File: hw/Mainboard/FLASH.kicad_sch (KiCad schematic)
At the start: 5 parts, among them J8 FLASH, U16 W25Q128JVS

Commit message: hw: add more Mouse part numbers
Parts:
- J8: MOUSER (none) -> 649-1012937893602BLF
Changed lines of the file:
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@@
+      (effects (font (size 1.27 1.27)) hide)
+    )
+    (property "MOUSER" "649-1012937893602BLF" (id 4) (at 107.95 114.3 0)
       (effects (font (size 1.27 1.27)) hide)
     )

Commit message: hw: 9V DC plug on left edge, change default track size
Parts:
- renumbered C51 to C85, J8 to J26, R25 to R72, R26 to R73, U16 to U22
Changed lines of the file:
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@@
   (symbol (lib_id "power:GND") (at 142.24 115.57 0) (unit 1)
     (in_bom yes) (on_board yes) (fields_autoplaced)
-    (property "Reference" "#PWR079" (id 0) (at 142.24 121.92 0)
+    (property "Reference" "#PWR0156" (id 0) (at 142.24 121.92 0)
       (effects (font (size 1.27 1.27)) hide)
     )
@@
   (symbol (lib_id "Device:R_Small") (at 127 88.9 0) (unit 1)
     (in_bom yes) (on_board yes)
-    (property "Reference" "R25" (id 0) (at 125.095 90.805 90)
+    (property "Reference" "R72" (id 0) (at 125.095 90.805 90)
       (effects (font (size 1.27 1.27)) (justify left))
     )
@@
   (symbol (lib_id "power:+3V3") (at 127 85.09 0) (unit 1)
     (in_bom yes) (on_board yes) (fields_autoplaced)
-    (property "Reference" "#PWR077" (id 0) (at 127 88.9 0)
+    (property "Reference" "#PWR0155" (id 0) (at 127 88.9 0)
       (effects (font (size 1.27 1.27)) hide)
     )
@@
   (symbol (lib_id "Device:R_Small") (at 116.84 101.6 180) (unit 1)
     (in_bom yes) (on_board yes)
-    (property "Reference" "R26" (id 0) (at 114.935 99.695 90)
+    (property "Reference" "R73" (id 0) (at 114.935 99.695 90)
       (effects (font (size 1.27 1.27)) (justify left))
     )
@@
   (symbol (lib_id "Device:C_Small") (at 146.05 78.74 0) (unit 1)
     (in_bom yes) (on_board yes)
-    (property "Reference" "C51" (id 0) (at 148.3868 77.5716 0)
+    (property "Reference" "C85" (id 0) (at 148.3868 77.5716 0)
       (effects (font (size 1.27 1.27)) (justify left))
     )
@@
   (symbol (lib_id "Memory_Flash:W25Q128JVS") (at 142.24 96.52 0) (unit 1)
     (in_bom yes) (on_board yes)
-    (property "Reference" "U16" (id 0) (at 133.35 87.63 0)
+    (property "Reference" "U22" (id 0) (at 133.35 87.63 0)
       (effects (font (size 1.27 1.27)) (justify left))
     )
@@
   (symbol (lib_id "Connector:Conn_01x02_Male") (at 107.95 114.3 0) (mirror x) (unit 1)
     (in_bom yes) (on_board yes) (fields_autoplaced)
-    (property "Reference" "J8" (id 0) (at 106.68 111.7599 0)
+    (property "Reference" "J26" (id 0) (at 106.68 111.7599 0)
       (effects (font (size 1.27 1.27)) (justify right))
     )
@@
   (symbol (lib_id "power:GND") (at 146.05 81.28 0) (unit 1)
     (in_bom yes) (on_board yes) (fields_autoplaced)
-    (property "Reference" "#PWR072" (id 0) (at 146.05 87.63 0)
+    (property "Reference" "#PWR0154" (id 0) (at 146.05 87.63 0)
       (effects (font (size 1.27 1.27)) hide)
     )
@@
   (symbol (lib_id "power:+3V3") (at 142.24 73.66 0) (unit 1)
     (in_bom yes) (on_board yes) (fields_autoplaced)
-    (property "Reference" "#PWR068" (id 0) (at 142.24 77.47 0)
+    (property "Reference" "#PWR0153" (id 0) (at 142.24 77.47 0)
       (effects (font (size 1.27 1.27)) hide)
     )

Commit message: hw: 25x2 header (wip)
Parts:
- renumbered J26 to J27
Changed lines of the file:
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@@
   (symbol (lib_id "power:GND") (at 142.24 115.57 0) (unit 1)
     (in_bom yes) (on_board yes) (fields_autoplaced)
-    (property "Reference" "#PWR0156" (id 0) (at 142.24 121.92 0)
+    (property "Reference" "#PWR0158" (id 0) (at 142.24 121.92 0)
       (effects (font (size 1.27 1.27)) hide)
     )
@@
   (symbol (lib_id "power:+3V3") (at 127 85.09 0) (unit 1)
     (in_bom yes) (on_board yes) (fields_autoplaced)
-    (property "Reference" "#PWR0155" (id 0) (at 127 88.9 0)
+    (property "Reference" "#PWR0157" (id 0) (at 127 88.9 0)
       (effects (font (size 1.27 1.27)) hide)
     )
@@
   (symbol (lib_id "Connector:Conn_01x02_Male") (at 107.95 114.3 0) (mirror x) (unit 1)
     (in_bom yes) (on_board yes) (fields_autoplaced)
-    (property "Reference" "J26" (id 0) (at 106.68 111.7599 0)
+    (property "Reference" "J27" (id 0) (at 106.68 111.7599 0)
       (effects (font (size 1.27 1.27)) (justify right))
     )
@@
   (symbol (lib_id "power:GND") (at 146.05 81.28 0) (unit 1)
     (in_bom yes) (on_board yes) (fields_autoplaced)
-    (property "Reference" "#PWR0154" (id 0) (at 146.05 87.63 0)
+    (property "Reference" "#PWR0156" (id 0) (at 146.05 87.63 0)
       (effects (font (size 1.27 1.27)) hide)
     )
@@
   (symbol (lib_id "power:+3V3") (at 142.24 73.66 0) (unit 1)
     (in_bom yes) (on_board yes) (fields_autoplaced)
-    (property "Reference" "#PWR0153" (id 0) (at 142.24 77.47 0)
+    (property "Reference" "#PWR0155" (id 0) (at 142.24 77.47 0)
       (effects (font (size 1.27 1.27)) hide)
     )

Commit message: hw: 2x config switch (wip)
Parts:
- renumbered J27 to J26
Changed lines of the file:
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@@
   (symbol (lib_id "power:GND") (at 142.24 115.57 0) (unit 1)
     (in_bom yes) (on_board yes) (fields_autoplaced)
-    (property "Reference" "#PWR0158" (id 0) (at 142.24 121.92 0)
+    (property "Reference" "#PWR0164" (id 0) (at 142.24 121.92 0)
       (effects (font (size 1.27 1.27)) hide)
     )
@@
   (symbol (lib_id "power:+3V3") (at 127 85.09 0) (unit 1)
     (in_bom yes) (on_board yes) (fields_autoplaced)
-    (property "Reference" "#PWR0157" (id 0) (at 127 88.9 0)
+    (property "Reference" "#PWR0163" (id 0) (at 127 88.9 0)
       (effects (font (size 1.27 1.27)) hide)
     )
@@
   (symbol (lib_id "Connector:Conn_01x02_Male") (at 107.95 114.3 0) (mirror x) (unit 1)
     (in_bom yes) (on_board yes) (fields_autoplaced)
-    (property "Reference" "J27" (id 0) (at 106.68 111.7599 0)
+    (property "Reference" "J26" (id 0) (at 106.68 111.7599 0)
       (effects (font (size 1.27 1.27)) (justify right))
     )
@@
   (symbol (lib_id "power:GND") (at 146.05 81.28 0) (unit 1)
     (in_bom yes) (on_board yes) (fields_autoplaced)
-    (property "Reference" "#PWR0156" (id 0) (at 146.05 87.63 0)
+    (property "Reference" "#PWR0162" (id 0) (at 146.05 87.63 0)
       (effects (font (size 1.27 1.27)) hide)
     )
@@
   (symbol (lib_id "power:+3V3") (at 142.24 73.66 0) (unit 1)
     (in_bom yes) (on_board yes) (fields_autoplaced)
-    (property "Reference" "#PWR0155" (id 0) (at 142.24 77.47 0)
+    (property "Reference" "#PWR0161" (id 0) (at 142.24 77.47 0)
       (effects (font (size 1.27 1.27)) hide)
     )

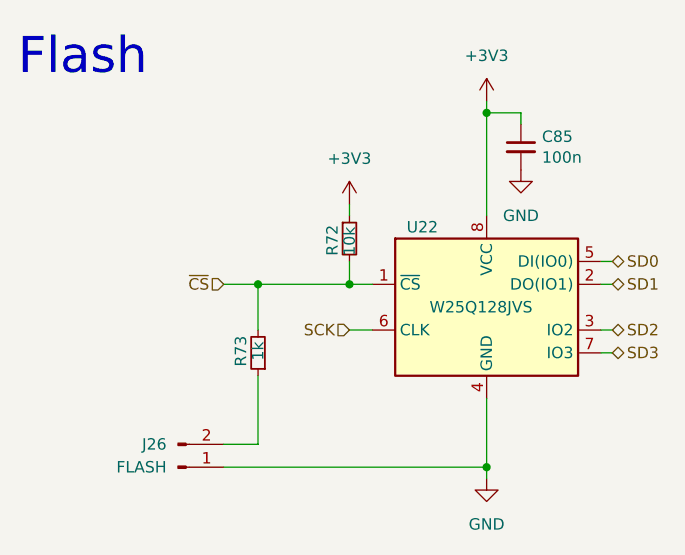
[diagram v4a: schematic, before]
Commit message: hw: header_and_jumper, button for flashing (wip)
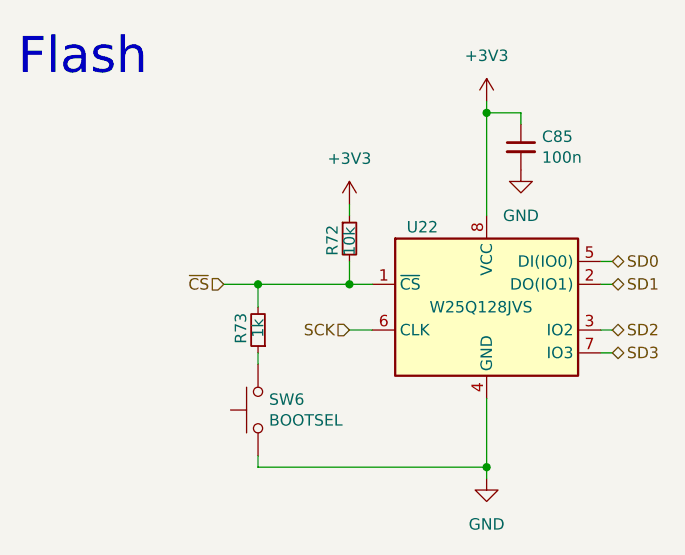
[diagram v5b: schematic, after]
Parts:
- removed J26: FLASH, Connector_PinHeader_2.54mm:PinHeader_1x02_P2.54mm_Vertical, symbol Connector:Conn_01x02_Male
- added SW6: BOOTSEL, JLCPCB:SW-TH_L6.0-W3.5-P6.50, symbol Switch:SW_Push
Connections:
- net GND: now also SW6.1
- net at R73.1: now also SW6.2
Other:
- moved on the sheet: R73
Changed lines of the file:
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@@
     (title "CBM PET Mainboard Replacement")
   )
+  (junction (at 127 93.98) (diameter 0) (color 0 0 0 0)
+  )
+  (junction (at 116.84 93.98) (diameter 0) (color 0 0 0 0)
+  )
   (junction (at 142.24 114.3) (diameter 0) (color 0 0 0 0)
   )
-  (junction (at 127 93.98) (diameter 0) (color 0 0 0 0)
-  )
-  (junction (at 116.84 93.98) (diameter 0) (color 0 0 0 0)
-  )
   (junction (at 142.24 74.93) (diameter 0) (color 0 0 0 0)
   )
+  (wire (pts (xy 116.84 113.03) (xy 116.84 114.3))
+    (stroke (width 0) (type default) (color 0 0 0 0))
+  )
+  (wire (pts (xy 142.24 114.3) (xy 142.24 115.57))
+    (stroke (width 0) (type default) (color 0 0 0 0))
+  )
   (wire (pts (xy 156.21 93.98) (xy 154.94 93.98))
     (stroke (width 0) (type default) (color 0 0 0 0))
   )
-  (wire (pts (xy 116.84 93.98) (xy 116.84 99.06))
+  (wire (pts (xy 116.84 93.98) (xy 116.84 96.52))
     (stroke (width 0) (type default) (color 0 0 0 0))
   )
@@
     (stroke (width 0) (type default) (color 0 0 0 0))
   )
-  (wire (pts (xy 113.03 114.3) (xy 142.24 114.3))
-    (stroke (width 0) (type default) (color 0 0 0 0))
-  )
-  (wire (pts (xy 142.24 114.3) (xy 142.24 115.57))
+  (wire (pts (xy 116.84 114.3) (xy 142.24 114.3))
     (stroke (width 0) (type default) (color 0 0 0 0))
   )
@@
     (stroke (width 0) (type default) (color 0 0 0 0))
   )
+  (wire (pts (xy 116.84 101.6) (xy 116.84 102.87))
+    (stroke (width 0) (type default) (color 0 0 0 0))
+  )
   (wire (pts (xy 116.84 93.98) (xy 127 93.98))
     (stroke (width 0) (type default) (color 0 0 0 0))
@@
     (stroke (width 0) (type default) (color 0 0 0 0))
   )
-  (wire (pts (xy 113.03 111.76) (xy 116.84 111.76))
-    (stroke (width 0) (type default) (color 0 0 0 0))
-  )
   (wire (pts (xy 113.03 93.98) (xy 116.84 93.98))
     (stroke (width 0) (type default) (color 0 0 0 0))
   )
   (wire (pts (xy 142.24 74.93) (xy 146.05 74.93))
-    (stroke (width 0) (type default) (color 0 0 0 0))
-  )
-  (wire (pts (xy 116.84 104.14) (xy 116.84 111.76))
     (stroke (width 0) (type default) (color 0 0 0 0))
   )
@@
   (hierarchical_label "~{CS}" (shape input) (at 113.03 93.98 180)
     (effects (font (size 1.27 1.27)) (justify right))
+  )
+  (symbol (lib_id "Switch:SW_Push") (at 116.84 107.95 90) (unit 1)
+    (in_bom yes) (on_board yes)
+    (property "Reference" "SW6" (id 0) (at 118.0592 106.7816 90)
+      (effects (font (size 1.27 1.27)) (justify right))
+    )
+    (property "Value" "BOOTSEL" (id 1) (at 118.0592 109.093 90)
+      (effects (font (size 1.27 1.27)) (justify right))
+    )
+    (property "Footprint" "JLCPCB:SW-TH_L6.0-W3.5-P6.50" (id 2) (at 111.76 107.95 0)
+      (effects (font (size 1.27 1.27)) hide)
+    )
+    (property "Datasheet" "" (id 3) (at 111.76 107.95 0)
+      (effects (font (size 1.27 1.27)) hide)
+    )
+    (property "LCSC" "" (id 4) (at 116.84 107.95 90)
+      (effects (font (size 1.27 1.27)) hide)
+    )
+    (property "Amazon" "https://smile.amazon.com/dp/B008DS188Y" (id 5) (at 116.84 107.95 90)
+      (effects (font (size 1.27 1.27)) hide)
+    )
+    (property "Alt-LCSC" "C457531" (id 6) (at 116.84 107.95 0)
+      (effects (font (size 1.27 1.27)) hide)
+    )
+    (property "MOUSER" "611-PTS636SK43LFS" (id 7) (at 116.84 107.95 0)
+      (effects (font (size 1.27 1.27)) hide)
+    )
+    (pin "1")
+    (pin "2")
   )
   (symbol (lib_id "power:GND") (at 142.24 115.57 0) (unit 1)
@@
     (pin "1")
   )
-  (symbol (lib_id "Device:R_Small") (at 116.84 101.6 180) (unit 1)
-    (in_bom yes) (on_board yes)
-    (property "Reference" "R73" (id 0) (at 114.935 99.695 90)
-      (effects (font (size 1.27 1.27)) (justify left))
-    )
-    (property "Value" "1k" (id 1) (at 116.84 100.33 90)
-      (effects (font (size 1.27 1.27)) (justify left))
-    )
-    (property "Footprint" "Resistor_SMD:R_0402_1005Metric" (id 2) (at 116.84 101.6 0)
-      (effects (font (size 1.27 1.27)) hide)
-    )
-    (property "Datasheet" "https://datasheet.lcsc.com/lcsc/2206010216_UNI-ROYAL-Uniroyal-Elec-0402WGF1001TCE_C11702.pdf" (id 3) (at 116.84 101.6 0)
-      (effects (font (size 1.27 1.27)) hide)
-    )
-    (property "LCSC" "C11702" (id 4) (at 116.84 101.6 0)
+  (symbol (lib_id "Device:R_Small") (at 116.84 99.06 180) (unit 1)
+    (in_bom yes) (on_board yes)
+    (property "Reference" "R73" (id 0) (at 114.935 97.155 90)
+      (effects (font (size 1.27 1.27)) (justify left))
+    )
+    (property "Value" "1k" (id 1) (at 116.84 97.79 90)
+      (effects (font (size 1.27 1.27)) (justify left))
+    )
+    (property "Footprint" "Resistor_SMD:R_0402_1005Metric" (id 2) (at 116.84 99.06 0)
+      (effects (font (size 1.27 1.27)) hide)
+    )
+    (property "Datasheet" "https://datasheet.lcsc.com/lcsc/2206010216_UNI-ROYAL-Uniroyal-Elec-0402WGF1001TCE_C11702.pdf" (id 3) (at 116.84 99.06 0)
+      (effects (font (size 1.27 1.27)) hide)
+    )
+    (property "LCSC" "C11702" (id 4) (at 116.84 99.06 0)
       (effects (font (size 1.27 1.27)) hide)
     )
@@
     (pin "8")
   )
-  (symbol (lib_id "Connector:Conn_01x02_Male") (at 107.95 114.3 0) (mirror x) (unit 1)
-    (in_bom yes) (on_board yes) (fields_autoplaced)
-    (property "Reference" "J26" (id 0) (at 106.68 111.7599 0)
-      (effects (font (size 1.27 1.27)) (justify right))
-    )
-    (property "Value" "FLASH" (id 1) (at 106.68 114.2999 0)
-      (effects (font (size 1.27 1.27)) (justify right))
-    )
-    (property "Footprint" "Connector_PinHeader_2.54mm:PinHeader_1x02_P2.54mm_Vertical" (id 2) (at 107.95 114.3 0)
-      (effects (font (size 1.27 1.27)) hide)
-    )
-    (property "Datasheet" "" (id 3) (at 107.95 114.3 0)
-      (effects (font (size 1.27 1.27)) hide)
-    )
-    (property "MOUSER" "649-1012937893602BLF" (id 4) (at 107.95 114.3 0)
-      (effects (font (size 1.27 1.27)) hide)
-    )
-    (pin "1")
-    (pin "2")
-  )
   (symbol (lib_id "power:GND") (at 146.05 81.28 0) (unit 1)

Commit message: hw: caps & logos (wip)
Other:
- title: CBM PET Mainboard Replacement -> EconoPET 40/8096
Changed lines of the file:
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@@
   (paper "A")
   (title_block
-    (title "CBM PET Mainboard Replacement")
+    (title "EconoPET 40/8096")
+    (date "2023-10-01")
+    (rev "A")
   )
   (junction (at 127 93.98) (diameter 0) (color 0 0 0 0)

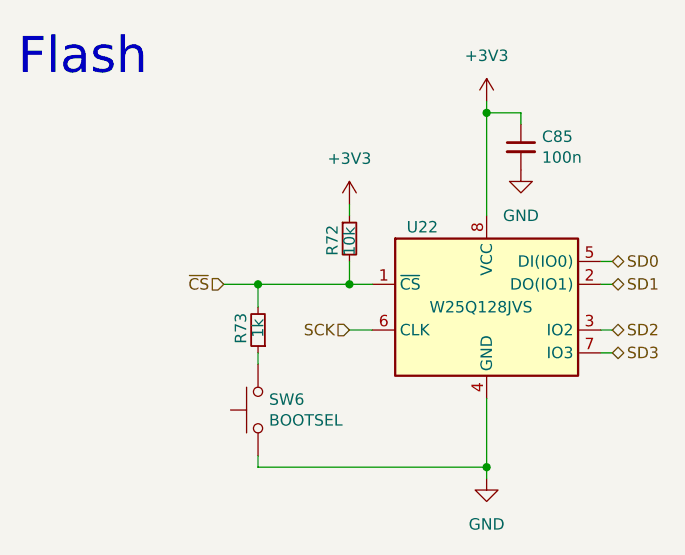
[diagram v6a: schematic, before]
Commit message: hw: renumber J* refs to match PET connectors
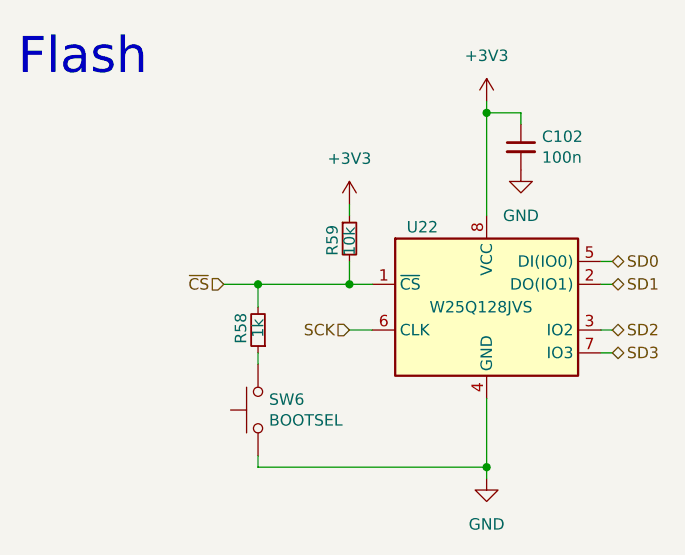
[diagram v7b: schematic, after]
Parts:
- renumbered C85 to C102, R73 to R58, R72 to R59
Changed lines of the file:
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@@
   (symbol (lib_id "power:GND") (at 142.24 115.57 0) (unit 1)
     (in_bom yes) (on_board yes) (fields_autoplaced)
-    (property "Reference" "#PWR0164" (id 0) (at 142.24 121.92 0)
+    (property "Reference" "#PWR0176" (id 0) (at 142.24 121.92 0)
       (effects (font (size 1.27 1.27)) hide)
     )
@@
   (symbol (lib_id "Device:R_Small") (at 127 88.9 0) (unit 1)
     (in_bom yes) (on_board yes)
-    (property "Reference" "R72" (id 0) (at 125.095 90.805 90)
+    (property "Reference" "R59" (id 0) (at 125.095 90.805 90)
       (effects (font (size 1.27 1.27)) (justify left))
     )
@@
   (symbol (lib_id "power:+3V3") (at 127 85.09 0) (unit 1)
     (in_bom yes) (on_board yes) (fields_autoplaced)
-    (property "Reference" "#PWR0163" (id 0) (at 127 88.9 0)
+    (property "Reference" "#PWR0174" (id 0) (at 127 88.9 0)
       (effects (font (size 1.27 1.27)) hide)
     )
@@
   (symbol (lib_id "Device:R_Small") (at 116.84 99.06 180) (unit 1)
     (in_bom yes) (on_board yes)
-    (property "Reference" "R73" (id 0) (at 114.935 97.155 90)
+    (property "Reference" "R58" (id 0) (at 114.935 97.155 90)
       (effects (font (size 1.27 1.27)) (justify left))
     )
@@
   (symbol (lib_id "Device:C_Small") (at 146.05 78.74 0) (unit 1)
     (in_bom yes) (on_board yes)
-    (property "Reference" "C85" (id 0) (at 148.3868 77.5716 0)
+    (property "Reference" "C102" (id 0) (at 148.3868 77.5716 0)
       (effects (font (size 1.27 1.27)) (justify left))
     )
@@
   (symbol (lib_id "power:GND") (at 146.05 81.28 0) (unit 1)
     (in_bom yes) (on_board yes) (fields_autoplaced)
-    (property "Reference" "#PWR0162" (id 0) (at 146.05 87.63 0)
+    (property "Reference" "#PWR0177" (id 0) (at 146.05 87.63 0)
       (effects (font (size 1.27 1.27)) hide)
     )
@@
   (symbol (lib_id "power:+3V3") (at 142.24 73.66 0) (unit 1)
     (in_bom yes) (on_board yes) (fields_autoplaced)
-    (property "Reference" "#PWR0161" (id 0) (at 142.24 77.47 0)
+    (property "Reference" "#PWR0175" (id 0) (at 142.24 77.47 0)
       (effects (font (size 1.27 1.27)) hide)
     )
